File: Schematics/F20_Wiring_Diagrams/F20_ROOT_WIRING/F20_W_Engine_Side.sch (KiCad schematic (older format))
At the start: 11 parts

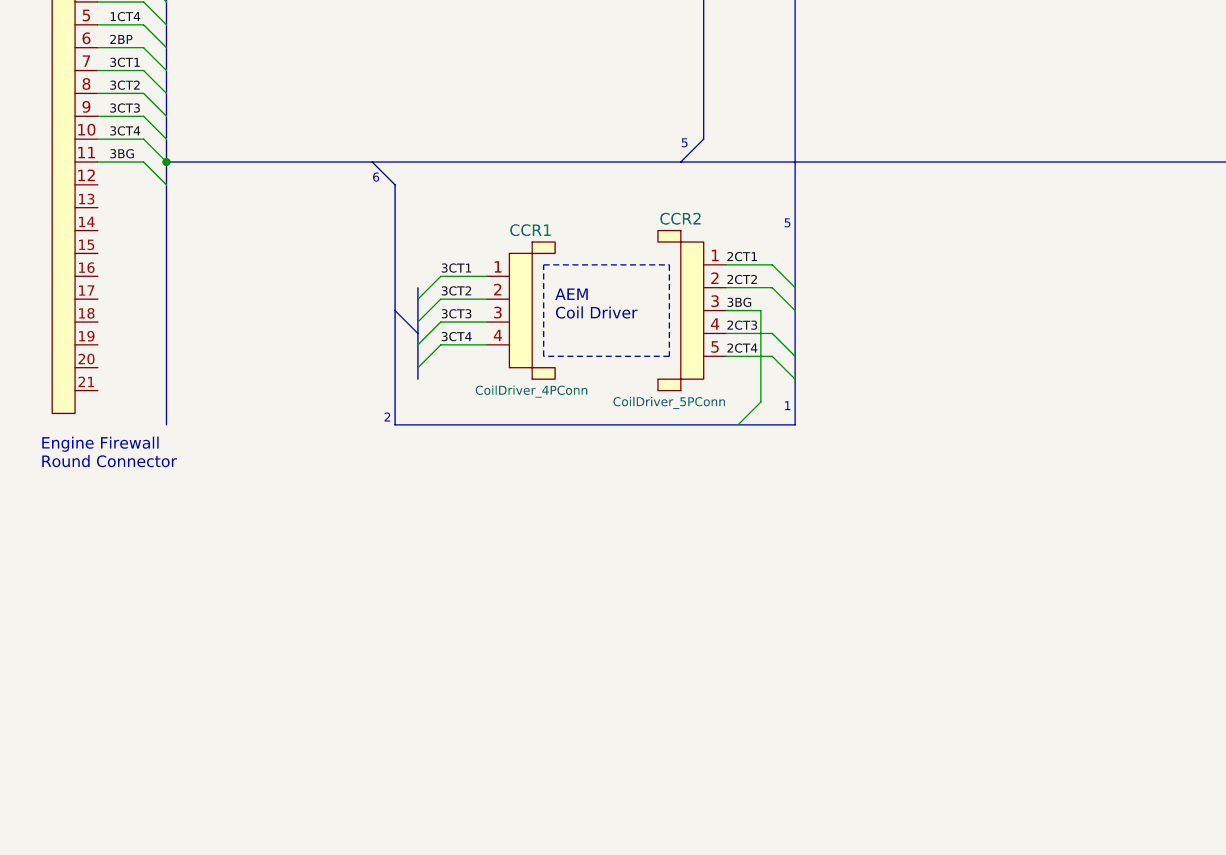
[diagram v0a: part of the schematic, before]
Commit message: Added fan/fuel pump wiring
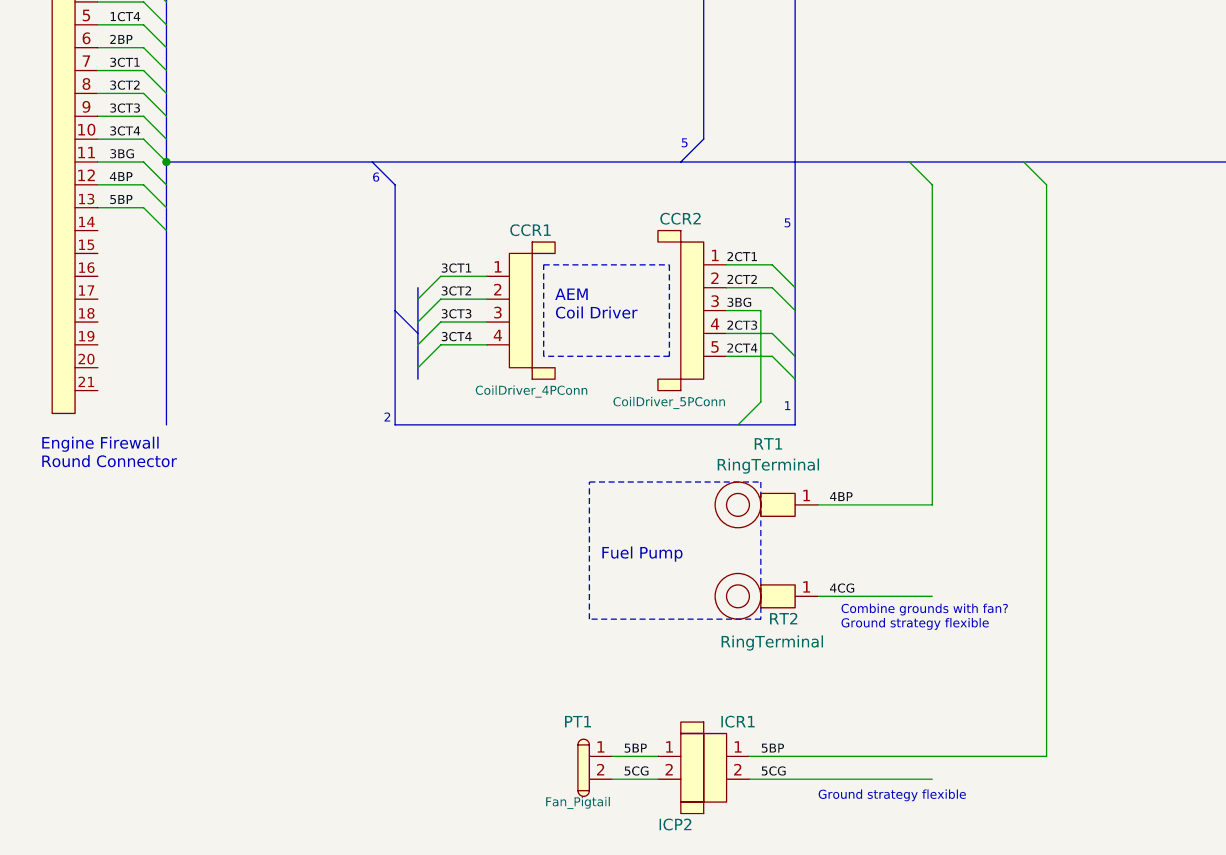
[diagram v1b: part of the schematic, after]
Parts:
- added ICP2: DTM06-2S, symbol FSAE_Library:DTM06-2S
- added ICR1: DTM04-2P, symbol FSAE_Library:DTM04-2P
- added PT1: Fan_Pigtail, symbol FSAE_Library:Fan_Pigtail
- added RT1, RT2: RingTerminal, symbol FSAE_Library:RingTerminal
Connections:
- net labels added: 4BP, 4CG, 5BP, 5CG
- wire segments 45 -> 55
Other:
- note added: "Combine grounds with fan?\nGround strategy flexible"
- note added: "Fuel Pump"
- note added: "Ground strategy flexible"
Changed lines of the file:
@@
 Text Label 4600 7650 0    39   ~ 0
 3BG
+$Comp
+L FSAE_Library:RingTerminal RT1
+U 1 1 5EEC8A28
+P 5000 8500
+F 0 "RT1" H 4783 8765 50  0000 C CNN
+F 1 "RingTerminal" H 4783 8674 50  0000 C CNN
+F 2 "" H 5000 8600 50  0001 C CNN
+F 3 "" H 5000 8600 50  0001 C CNN
+	1    5000 8500
+	1    0    0    -1
+$EndComp
+$Comp
+L FSAE_Library:RingTerminal RT2
+U 1 1 5EEC93A2
+P 5000 8900
+F 0 "RT2" H 4850 8800 50  0000 C CNN
+F 1 "RingTerminal" H 4800 8700 50  0000 C CNN
+F 2 "" H 5000 9000 50  0001 C CNN
+F 3 "" H 5000 9000 50  0001 C CNN
+	1    5000 8900
+	1    0    0    -1
+$EndComp
+Wire Notes Line
+	4750 8400 4750 9000
+Wire Notes Line
+	4750 9000 4000 9000
+Wire Notes Line
+	4000 9000 4000 8400
+Wire Notes Line
+	4000 8400 4750 8400
+Text Notes 4050 8750 0    50   ~ 0
+Fuel Pump
+Wire Wire Line
+	5500 8500 5500 7100
+Wire Wire Line
+	5000 8500 5500 8500
+Entry Wire Line
+	5400 7000 5500 7100
+Text Label 5050 8500 0    39   ~ 0
+4BP
+Text Label 1900 7100 0    39   ~ 0
+4BP
+Wire Wire Line
+	1850 7100 2050 7100
+Entry Wire Line
+	2050 7100 2150 7200
+Wire Wire Line
+	5000 8900 5500 8900
+Text Label 5050 8900 0    39   ~ 0
+4CG
+$Comp
+L FSAE_Library:Fan_Pigtail PT1
+U 1 1 5EEE6E5F
+P 4000 9600
+F 0 "PT1" H 4050 9750 50  0000 C CNN
+F 1 "Fan_Pigtail" H 4050 9400 39  0000 C CNN
+F 2 "" H 4200 9700 50  0001 C CNN
+F 3 "" H 4200 9700 50  0001 C CNN
+	1    4000 9600
+	-1   0    0    -1
+$EndComp
+Wire Wire Line
+	4100 9600 4300 9600
+Wire Wire Line
+	4100 9700 4300 9700
+Wire Wire Line
+	4700 9700 5500 9700
+Text Notes 5000 9800 0    39   ~ 0
+Ground strategy flexible
+Text Notes 5100 9050 0    39   ~ 0
+Combine grounds with fan?\nGround strategy flexible
+Text Label 4150 9600 0    39   ~ 0
+5BP
+Text Label 4150 9700 0    39   ~ 0
+5CG
+Text Label 4750 9700 0    39   ~ 0
+5CG
+Text Label 4750 9600 0    39   ~ 0
+5BP
+Wire Wire Line
+	4700 9600 6000 9600
+Wire Wire Line
+	6000 9600 6000 7100
+Entry Wire Line
+	5900 7000 6000 7100
+Entry Wire Line
+	2050 7200 2150 7300
+Wire Wire Line
+	2050 7200 1850 7200
 Wire Bus Line
 	2150 7000 2150 8150
 Wire Bus Line
+	3150 8150 4900 8150
+Wire Bus Line
+	3250 7550 3250 7950
+Wire Bus Line
 	3150 7100 3150 8150
-Wire Bus Line
-	3150 8150 4900 8150
 Wire Bus Line
 	2150 7000 13000 7000
 Wire Bus Line
+	4900 4500 4900 8150
+Wire Bus Line
 	4500 4500 4500 6900
 Wire Bus Line
-	3250 7550 3250 7950
-Wire Bus Line
 	2150 6050 2150 7000
-Wire Bus Line
-	4900 4500 4900 8150
+$Comp
+L FSAE_Library:DTM04-2P ICR1
+U 1 1 5EEFFACE
+P 4700 9600
+F 0 "ICR1" H 4650 9750 50  0000 C CNN
+F 1 "DTM04-2P" H 4558 9824 50  0001 C CNN
+F 2 "" H 4700 9700 50  0001 C CNN
+F 3 "" H 4700 9700 50  0001 C CNN
+	1    4700 9600
+	1    0    0    -1
+$EndComp
+$Comp
+L FSAE_Library:DTM06-2S ICP2
+U 1 1 5EF001C2
+P 4400 9600
+F 0 "ICP2" H 4300 9300 50  0000 L CNN
+F 1 "DTM06-2S" H 4300 9200 50  0001 L CNN
+F 2 "" H 4600 9700 50  0001 C CNN
+F 3 "" H 4600 9700 50  0001 C CNN
+	1    4400 9600
+	1    0    0    -1
+$EndComp
+Text Label 1900 7200 0    39   ~ 0
+5BP
 $EndSCHEMATC
